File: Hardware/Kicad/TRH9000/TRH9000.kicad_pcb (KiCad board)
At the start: 4 copper layers, 99.1 x 79.7 mm, 109 parts, among them J1 Norcomp_200-015-263R001, J2 Console5_SCART, J5 DIN-8_SD-80BV, Q1 BC817, U1 V9990, U2 KM428C256, U3 KM428C256, U4 74VHC138, U5 T.I_SN74AHCT32D, U6 LMH1980, U7 T.I_SN74CBT3257, U8 LMH1980, U9 SST39SF010A-lrj, X1 Crystek_CE3291, Y1 Y_HCM4921477270ABJT

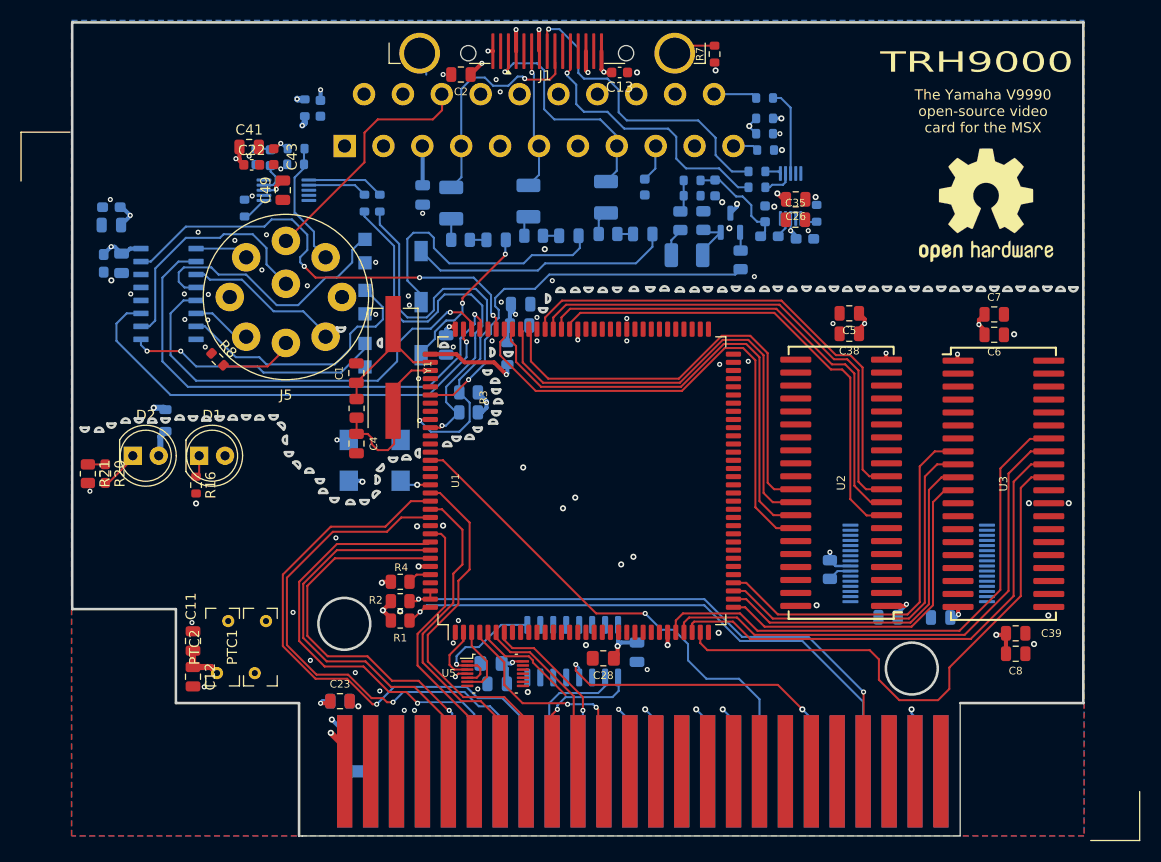
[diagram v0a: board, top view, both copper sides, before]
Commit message: Continued with routing - slowly getting the memory-lines done. Also finished up the SCART-connector.
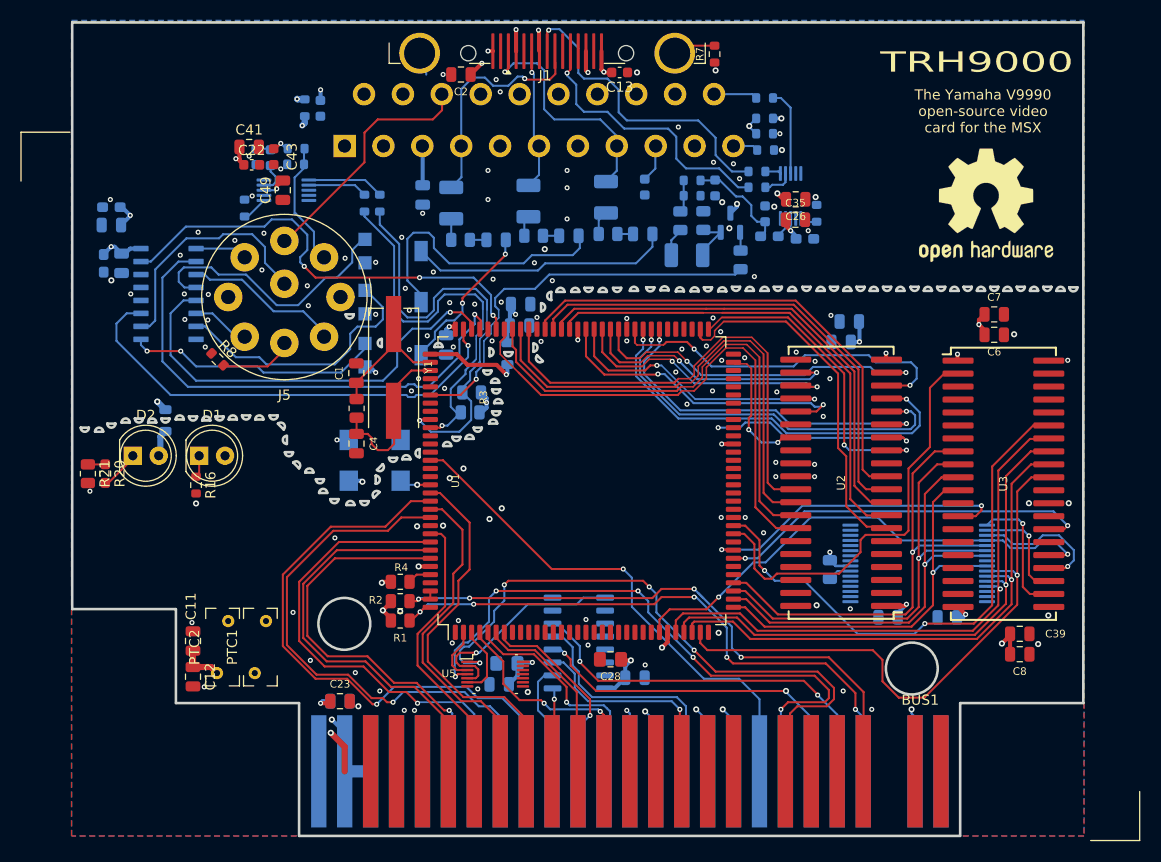
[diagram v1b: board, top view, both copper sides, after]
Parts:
- BUS1: footprint trh9000:msx_cart_edge-conn -> trh9000:msx_edge-conn-LP
- C38, C5: moved to B.Cu
- moved C29 2.51 mm to (153.4, 111.5), turned to 0 degrees
- moved C30 1.55 mm to (140.8, 110.1)
- moved C38 1.13 mm to (173.6, 78.6)
- moved U4 1.00 mm to (147.9, 108.1), turned to 0 degrees
- moved C5 0.80 mm to (174.4, 76.6)
- moved C28 0.71 mm to (151.0, 109.7)
- moved C45 0.65 mm to (184.0, 105.6)
- moved C39 0.40 mm to (191.1, 107.2)
- moved C8 0.40 mm to (191.1, 109.2)
- moved R5 0.30 mm to (137.4, 83.5)
- moved C31 0.21 mm to (140.1, 112.2)
- moved J5 0.15 mm to (119.0, 74.2)
- moved R6 0.15 mm to (137.2, 85.5)
- moved U5 0.05 mm to (139.7, 111.2)
- moved Y1 0.05 mm to (129.8, 81.1)
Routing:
- net /~{RD}: track 0.00 -> 62.4 mm, vias 0 -> 4
- net /~{WR}: track 1.30 -> 61.2 mm, vias 1 -> 5
- net /VDP/~{VO_SOE}: track 0.00 -> 53.2 mm, vias 0 -> 2
- net /VDP/V0A0: track 0.00 -> 49.4 mm, vias 0 -> 2
- net /VDP/~{V0_SC}: track 0.00 -> 41.2 mm
- net /VDP/V1A6: track 0.00 -> 40.4 mm, vias 0 -> 2
- net /VDP/V1A7: track 0.00 -> 38.2 mm, vias 0 -> 2
- net /~{M1}: track 0.00 -> 38.1 mm, vias 0 -> 2
- net /VDP/~{V0_CAS}: track 0.00 -> 37.2 mm, vias 0 -> 2
- net /VDP/~{V1_TR}: track 0.00 -> 35.7 mm
- net /VDP/V1A5: track 0.00 -> 35.4 mm, vias 0 -> 2
- net /VDP/V1A8: track 0.00 -> 34.7 mm, vias 0 -> 2
- net /VDP/V1A4: track 0.00 -> 34.2 mm, vias 0 -> 2
- net /VDP/~{V0_WE}: track 0.00 -> 31.4 mm, vias 0 -> 2
- net /VDP/~{V1_WE}: track 0.00 -> 31.3 mm, vias 0 -> 2
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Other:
- outline, holes or cut-outs redrawn
